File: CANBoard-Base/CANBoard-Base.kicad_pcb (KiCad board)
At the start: 4 copper layers, 62.2 x 73.8 mm, 110 parts, among them J1 DTM12 A, J2 DTM12 B, U1 CANBoard_v2, U2 LM324, U3 LM324, U4 SRV05-4, U5 SRV05-4, U6 SRV05-4, U7 SRV05-4, U8 LD1117S33CTR

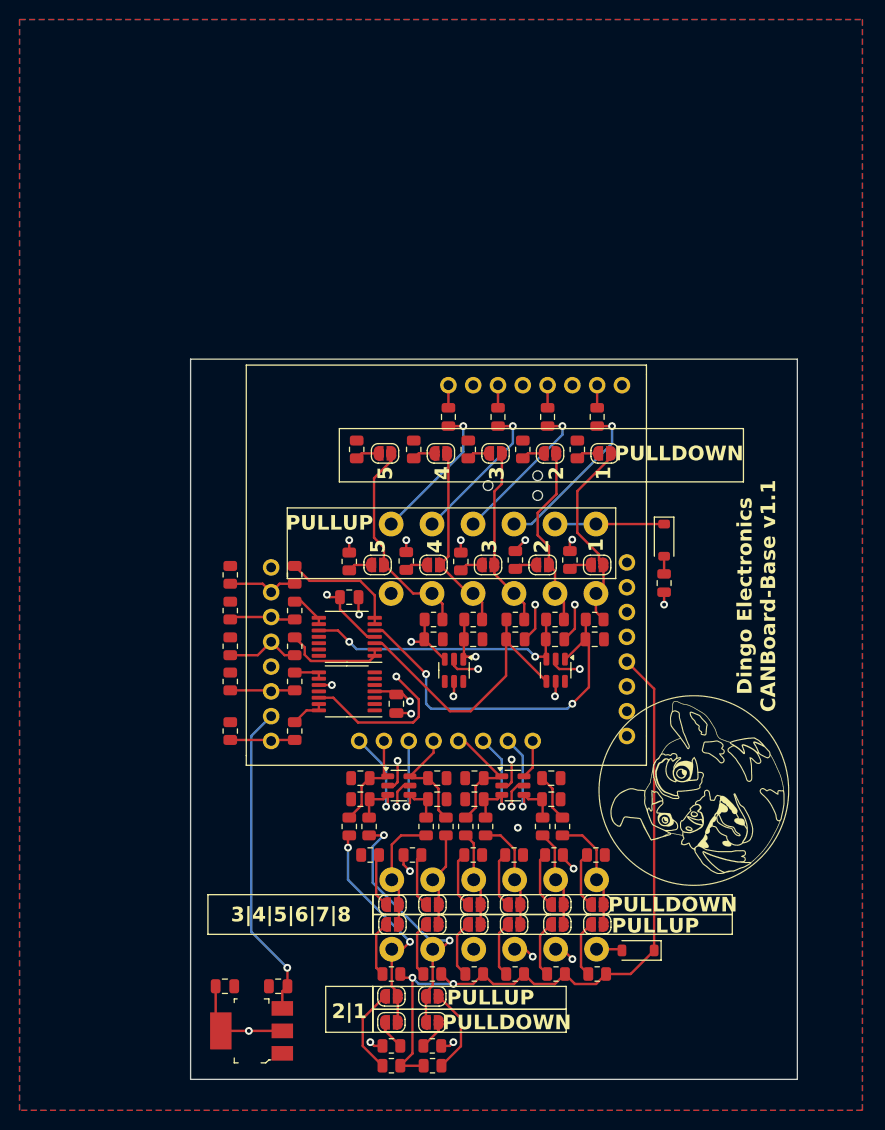
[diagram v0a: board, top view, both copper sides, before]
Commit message: silkscreen changes
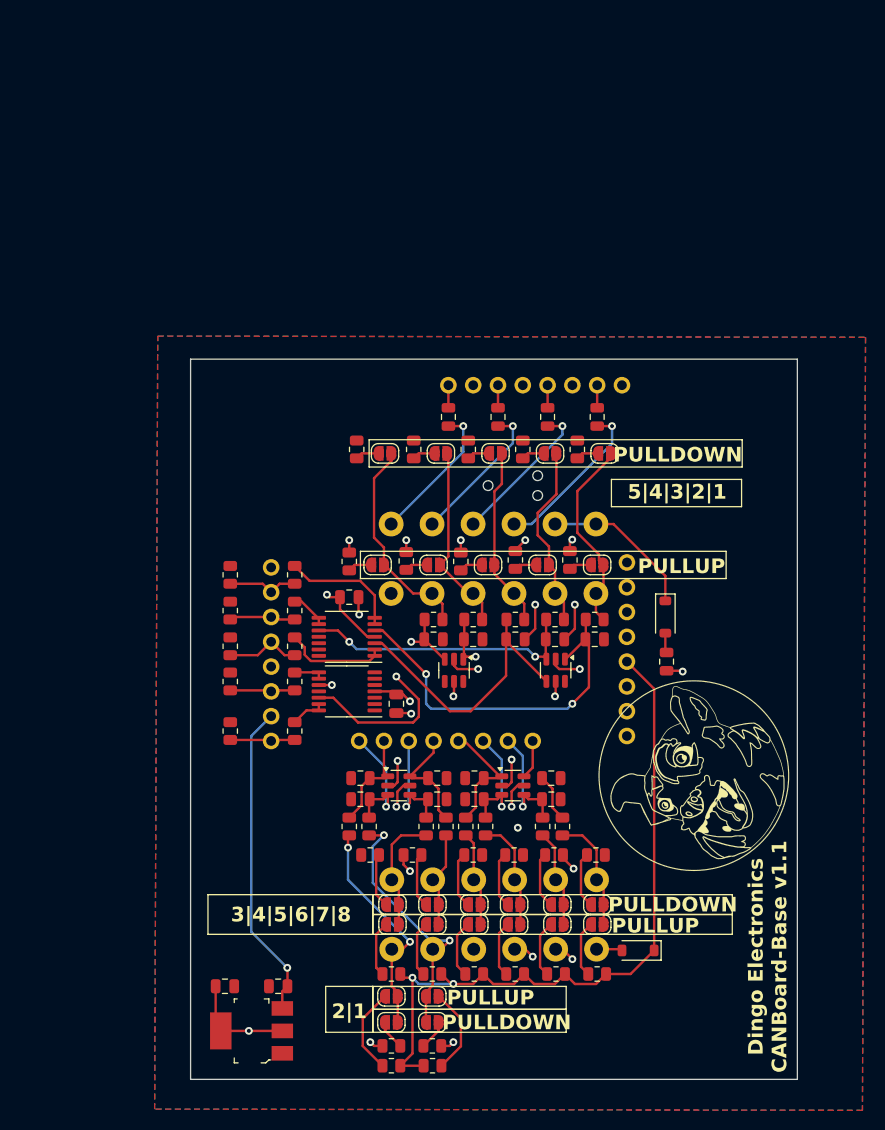
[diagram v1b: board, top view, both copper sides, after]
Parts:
- moved F1 8.05 mm to (4.06, -7.62)
- moved D2 7.88 mm to (3.94, -12.2)
- moved G1 1.52 mm to (6.86, 4.06)
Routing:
- net +5VP: track 11.2 -> 16.1 mm
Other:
- board text added: "5|4|3|2|1"
- board text added: "DTM A - GREY INSERT"
- board text added: "DTM B - BLACK INSERT"
- board text removed: "1"
- board text removed: "2"
- board text removed: "3"
- board text removed: "4"
- board text removed: "5"
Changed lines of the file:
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@@
 	(footprint "DRTLogo:DingoFaceNoFill"
 		(layer "F.Cu")
-		(at 6.858 5.588 90)
+		(at 6.858 4.064 90)
 		(property "Reference" "G1"
 			(at 12.192 4.064 90)
@@
 	(footprint "Diode_SMD:D_SOD-123"
 		(layer "F.Cu")
-		(at 3.81 -20.066 -90)
+		(at 3.937 -12.192 -90)
 		(descr "SOD-123")
 		(tags "SOD-123")
@@
 	(footprint "Fuse:Fuse_0805_2012Metric"
 		(layer "F.Cu")
-		(at 3.81 -15.6695 90)
+		(at 4.064 -7.62 90)
 		(descr "Fuse SMD 0805 (2012 Metric), square (rectangular) end terminal, IPC_7351 nominal, (Body size source: https://docs.google.com/spreadsheets/d/1BsfQQcO9C6DZCsRaXUlFlo91Tg2WpOkGARC1WS5S8t0/edit?usp=sharing), generated with kicad-footprint-generator")
 		(tags "fuse")
@@
 		(attr through_hole exclude_from_bom)
 		(fp_line
-			(start -39 -38)
-			(end -39 2)
-			(stroke
-				(width 0.12)
-				(type solid)
-			)
-			(layer "F.SilkS")
-		)
-		(fp_line
-			(start -39 2)
-			(end -39 3)
-			(stroke
-				(width 0.12)
-				(type solid)
-			)
-			(layer "F.SilkS")
-		)
-		(fp_line
-			(start -39 3)
-			(end 2 3)
-			(stroke
-				(width 0.12)
-				(type solid)
-			)
-			(layer "F.SilkS")
-		)
-		(fp_line
-			(start 2 -38)
-			(end -39 -38)
-			(stroke
-				(width 0.12)
-				(type solid)
-			)
-			(layer "F.SilkS")
-		)
-		(fp_line
-			(start 2 -37)
-			(end 2 -38)
-			(stroke
-				(width 0.12)
-				(type solid)
-			)
-			(layer "F.SilkS")
-		)
-		(fp_line
-			(start 2 0)
-			(end 2 -37)
-			(stroke
-				(width 0.12)
-				(type solid)
-			)
-			(layer "F.SilkS")
-		)
-		(fp_line
-			(start 2 3)
-			(end 2 0)
-			(stroke
-				(width 0.12)
-				(type solid)
-			)
-			(layer "F.SilkS")
-		)
-		(fp_line
 			(start -39.2 -38.2)
 			(end 2.2 -38.2)
@@
 	)
 	(gr_rect
-		(start -34.798 -23.368)
-		(end -1.143 -16.129)
+		(start -27.305 -18.923)
+		(end 10.16 -16.129)
 		(stroke
 			(width 0.12)
@@
 	)
 	(gr_rect
-		(start -29.464 -31.496)
-		(end 11.938 -26.035)
+		(start -1.5875 -26.289)
+		(end 11.7475 -23.495)
+		(stroke
+			(width 0.12)
+			(type default)
+		)
+		(fill none)
+		(layer "F.SilkS")
+	)
+	(gr_rect
+		(start -26.416 -30.353)
+		(end 11.811 -27.559)
 		(stroke
 			(width 0.12)
@@
 		(layer "Edge.Cuts")
 	)
-	(gr_text "Dingo Electronics\nCANBoard-Base v1.1"
-		(at 15.367 -14.351 90)
-		(layer "F.SilkS")
+	(gr_text "DTM A - GREY INSERT"
+		(at -14.732 -17.272 0)
+		(layer "B.SilkS")
 		(effects
 			(font
@@
 				(bold yes)
 			)
-			(justify bottom)
-		)
-	)
-	(gr_text "PULLDOWN"
-		(at 5.334 -28.067 0)
-		(layer "F.SilkS")
-		(effects
-			(font
-				(size 1.4986 1.4986)
-				(thickness 0.29972)
-				(bold yes)
-			)
-			(justify bottom)
-		)
-	)
-	(gr_text "2"
-		(at -6.35 -26.924 90)
-		(layer "F.SilkS")
-		(effects
-			(font
-				(size 1.4986 1.4986)
-				(thickness 0.29972)
-				(bold yes)
-			)
-			(justify bottom)
-		)
-	)
-	(gr_text "5"
-		(at -24.638 -19.431 90)
-		(layer "F.SilkS")
-		(effects
-			(font
-				(size 1.4986 1.4986)
-				(thickness 0.29972)
-				(bold yes)
-			)
-			(justify bottom)
+			(justify bottom mirror)
 		)
 	)
-	(gr_text "3"
-		(at -13.208 -19.431 90)
-		(layer "F.SilkS")
+	(gr_text "DTM B - BLACK INSERT"
+		(at -15.24 19.304 0)
+		(layer "B.SilkS")
 		(effects
 			(font
-				(size 1.4986 1.4986)
-				(thickness 0.29972)
-				(bold yes)
-			)
-			(justify bottom)
-		)
-	)
-	(gr_text "5"
-		(at -23.876 -26.924 90)
-		(layer "F.SilkS")
-		(effects
-			(font
-				(size 1.4986 1.4986)
-				(thickness 0.29972)
+				(size 1.5 1.5)
+				(thickness 0.3)
 				(bold yes)
 			)
-			(justify bottom)
+			(justify bottom mirror)
 		)
 	)
-	(gr_text "1"
-		(at -2.286 -19.558 90)
+	(gr_text "Dingo Electronics\nCANBoard-Base v1.1"
+		(at 16.51 22.606 90)
 		(layer "F.SilkS")
 		(effects
 			(font
-				(size 1.4986 1.4986)
-				(thickness 0.29972)
+				(size 1.5 1.5)
+				(thickness 0.3)
 				(bold yes)
 			)
@@
 		)
 	)
-	(gr_text "3"
-		(at -12.446 -26.924 90)
+	(gr_text "PULLDOWN"
+		(at 5.207 -27.94 0)
 		(layer "F.SilkS")
 		(effects
@@
 	)
 	(gr_text "PULLUP"
-		(at -30.48 -20.955 0)
-		(layer "F.SilkS")
-		(effects
-			(font
-				(size 1.4986 1.4986)
-				(thickness 0.29972)
-				(bold yes)
-			)
-			(justify bottom)
-		)
-	)
-	(gr_text "4"
-		(at -18.796 -19.431 90)
+		(at 5.588 -16.51 0)
 		(layer "F.SilkS")
 		(effects
@@
 		)
 	)
-	(gr_text "PULLUP"
-		(at 2.921 20.32 0)
-		(layer "F.SilkS")
-		(effects
-			(font
-				(size 1.4986 1.4986)
-				(thickness 0.29972)
-				(bold yes)
-			)
-			(justify bottom)
-		)
-	)
-	(gr_text "2"
-		(at -7.874 -19.431 90)
+	(gr_text "5|4|3|2|1"
+		(at 5.1435 -24.13 0)
 		(layer "F.SilkS")
 		(effects
@@
 		)
 	)
-	(gr_text "1"
-		(at -1.524 -26.924 90)
-		(layer "F.SilkS")
-		(effects
-			(font
-				(size 1.4986 1.4986)
-				(thickness 0.29972)
-				(bold yes)
-			)
-			(justify bottom)
-		)
-	)
-	(gr_text "4"
-		(at -18.034 -26.924 90)
+	(gr_text "PULLUP"
+		(at 2.921 20.32 0)
 		(layer "F.SilkS")
 		(effects
@@
 	)
 	(segment
-		(start -7.3 -4.13)
-		(end -7.366 -4.064)
+		(start 4.064 -6.6825)
+		(end 5.6365 -6.6825)
 		(width 0.25)
 		(layer "F.Cu")
@@
 	)
 	(segment
-		(start 3.81 -14.732)
-		(end 3.81 -13.462)
+		(start -7.3 -4.13)
+		(end -7.366 -4.064)
 		(width 0.25)
 		(layer "F.Cu")
@@
 	)
 	(segment
+		(start 5.6365 -6.6825)
+		(end 5.715 -6.604)
+		(width 0.25)
+		(layer "F.Cu")
+		(net 14)
+	)
+	(segment
 		(start -30.48 -14.224)
 		(end -30.734 -14.478)
@@
 	)
 	(via
-		(at 3.81 -13.462)
+		(at -17.78 -4.064)
 		(size 0.8)
 		(drill 0.4)
@@
 	)
 	(via
-		(at -17.78 -4.064)
+		(at 5.715 -6.604)
 		(size 0.8)
 		(drill 0.4)
@@
 	)
 	(segment
-		(start 3.809 -21.717)
-		(end 3.81 -21.716)
+		(start 3.937 -16.401051)
+		(end 3.937 -13.842)
+		(width 0.25)
+		(layer "F.Cu")
+		(net 17)
+	)
+	(segment
+		(start -1.378949 -21.717)
+		(end 3.937 -16.401051)
 		(width 0.25)
 		(layer "F.Cu")
@@
 	(segment
 		(start -3.175 -21.717)
-		(end 3.809 -21.717)
+		(end -1.378949 -21.717)
 		(width 0.25)
 		(layer "F.Cu")
@@
 	)
 	(segment
-		(start 3.81 -18.416)
-		(end 3.81 -16.607)
+		(start 3.937 -8.6845)
+		(end 4.064 -8.5575)
+		(width 0.25)
+		(layer "F.Cu")
+		(net 18)
+	)
+	(segment
+		(start 3.937 -10.542)
+		(end 3.937 -8.6845)
 		(width 0.25)
 		(layer "F.Cu")
@@
 		(polygon
 			(pts
-				(xy -62.23 -73.406) (xy 24.13 -73.406) (xy 24.13 38.354) (xy -62.23 38.354)
+				(xy -48.06996 -40.972499) (xy 24.44704 -40.845499) (xy 24.13 38.354) (xy -48.387 38.227)
 			)
 		)
@@
 		(polygon
 			(pts
-				(xy -62.992 -73.406) (xy 23.368 -73.406) (xy 23.368 38.354) (xy -62.992 38.354)
+				(xy -48.641 -41.91) (xy 24.13 -42.164) (xy 23.368 38.354) (xy -49.403 38.608)
 			)
 		)
